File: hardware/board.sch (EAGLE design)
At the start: 79 parts, among them CON1 USB-FPGA1.11, IC1 AD80XX

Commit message: Working on improved board revB Added DC-DC and selection jumper Added some libraries Fixed THS3062 symbol Split up sheets
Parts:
- removed CON_UC: (no value), con-molex:22-23-2061
- added CON2: USB-FPGA-2THT, usb-fpga-2:USB-FPGA-2THT
- added R7: 0R, rcl:R-EU_M0805
- added TP2, TP3, TP_GND2: TPPAD1-13, testpad:TPPAD1-13
- added U$6: IAS0105D09, xppower-IAS01:IAS0105D09
- IC1: value AD80XX -> THS3062; device ad80xx:AD80XX -> ths3062:THS3062
- JP1: device pinhead:PINHD-1X2 -> jumper:JP4Q
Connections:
- removed net N$60: CON1_CDF-FX2.C13~PE3/RXD0OUT, CON_UC-5.S
- removed net N$61: CON1_CDF-FX2.C14~PE2/T2OUT, CON_UC-4.S
- removed net N$62: CON1_CDF-FX2.C15~PE1/T1OUT, CON_UC-3.S
- removed net N$63: CON1_CDF-FX2.C16~PE0/T0OUT, CON_UC-2.S
- new net +9V: JP1.5, U$6.+VOUT
- new net -9V: JP1.7, U$6.-VOUT
- new net N$13: D2.C, JP1.3
- new net N$17: D1.A, JP1.1
- new net N$7: R7.1, U$6.0V
- net +5V: now also U$6.+VIN
- net +5V/3: no longer CON_UC-1.S
- net DAC_OUT_NET: now also TP2.TP; no longer JP1.1
- net GND: now also U$6.-VIN; no longer CON_UC-6.S
- net GND1: now also IC1THS3062OP2.IN+, R7.2, TP3.TP, TP_GND2.TP; no longer IC1AD80XXOP2.IN+, JP1.2
- net N$10: now also IC1THS3062OP1.IN+; no longer IC1AD80XXOP1.IN+
- net N$11: now also IC1THS3062OP1.IN-; no longer IC1AD80XXOP1.IN-
- net N$12: now also IC1THS3062OP1.OUT; no longer IC1AD80XXOP1.OUT
- net N$24: now also IC1THS3062OP2.IN-; no longer IC1AD80XXOP2.IN-
- net N$33: now also IC1THS3062OP2.OUT; no longer IC1AD80XXOP2.OUT
- net V+: no longer OP_VCC.3
- net V-: no longer OP_VCC.1
- net VCC+: now also JP1.4, JP1.6, OP_VCC.3; no longer D2.C
- net VCC-: now also JP1.2, JP1.8, OP_VCC.1; no longer D1.A
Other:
- note added: "Change to v2"
- note added: "Fix library"
- note added: "Gives the unamplified waveform"
- note added: "Power"
- note added: "Select internal/external supply"
- note added: "WARNING: If the FPGA is powered from USB, then the voltage after the reg is usually too low (measured 4.85V) Best is to power FPGA from supply"
- note added: "angled connector? screw connector?"

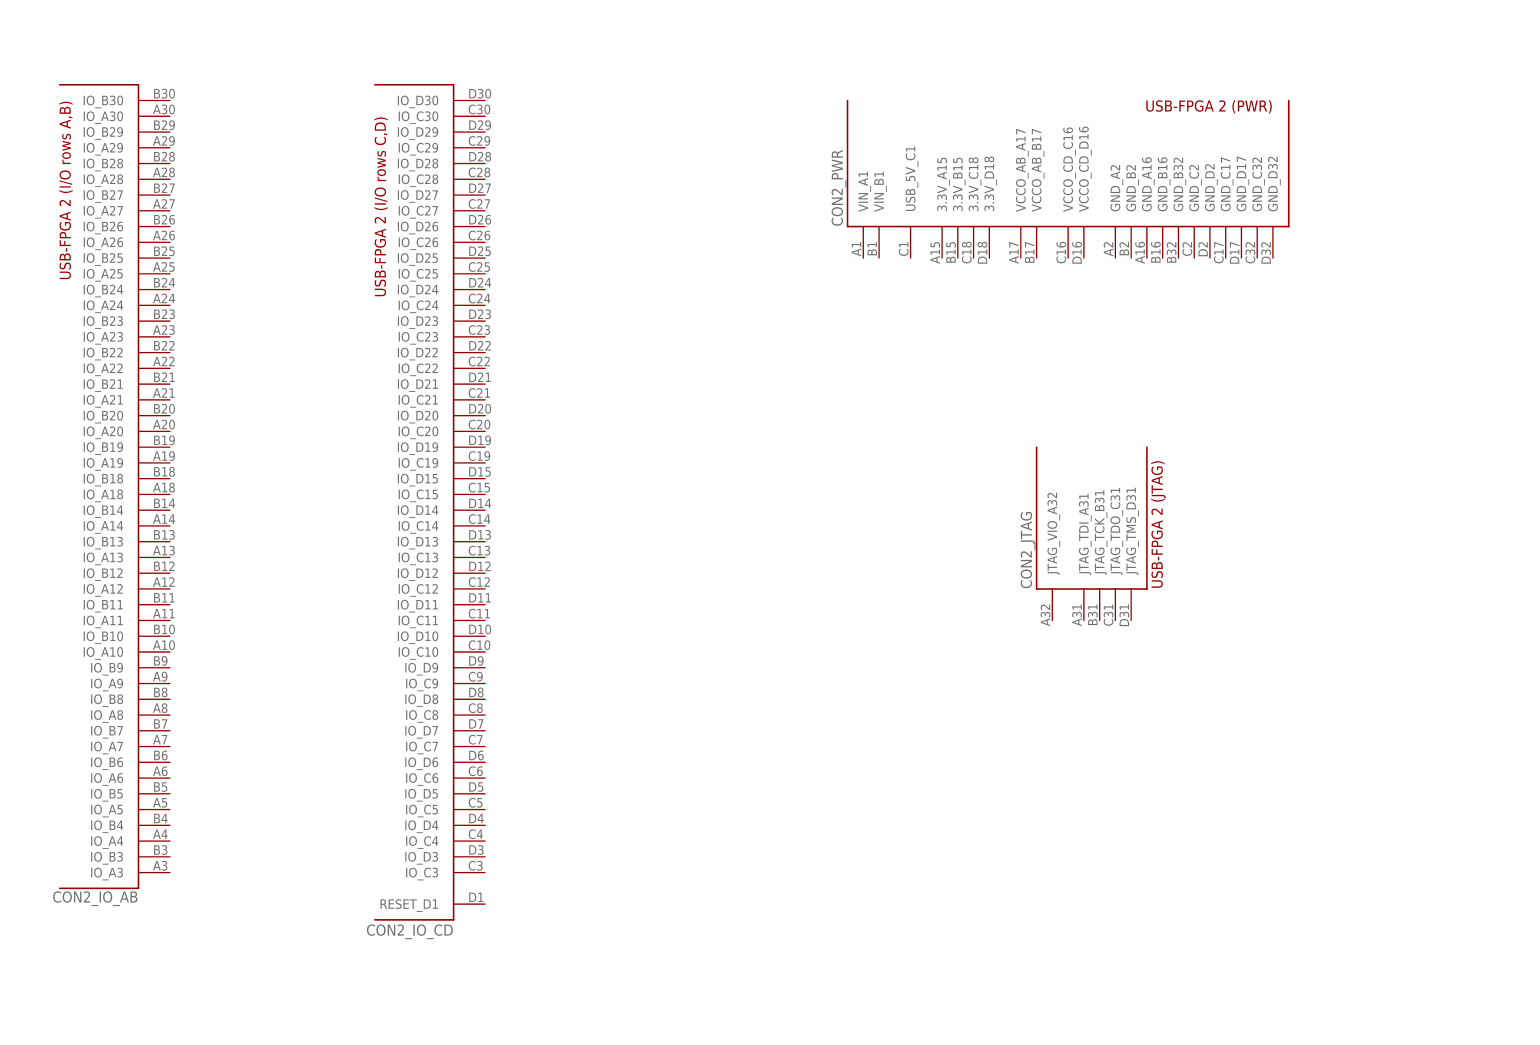
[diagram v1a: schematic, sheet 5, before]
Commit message: Working on change to new v2 pinout
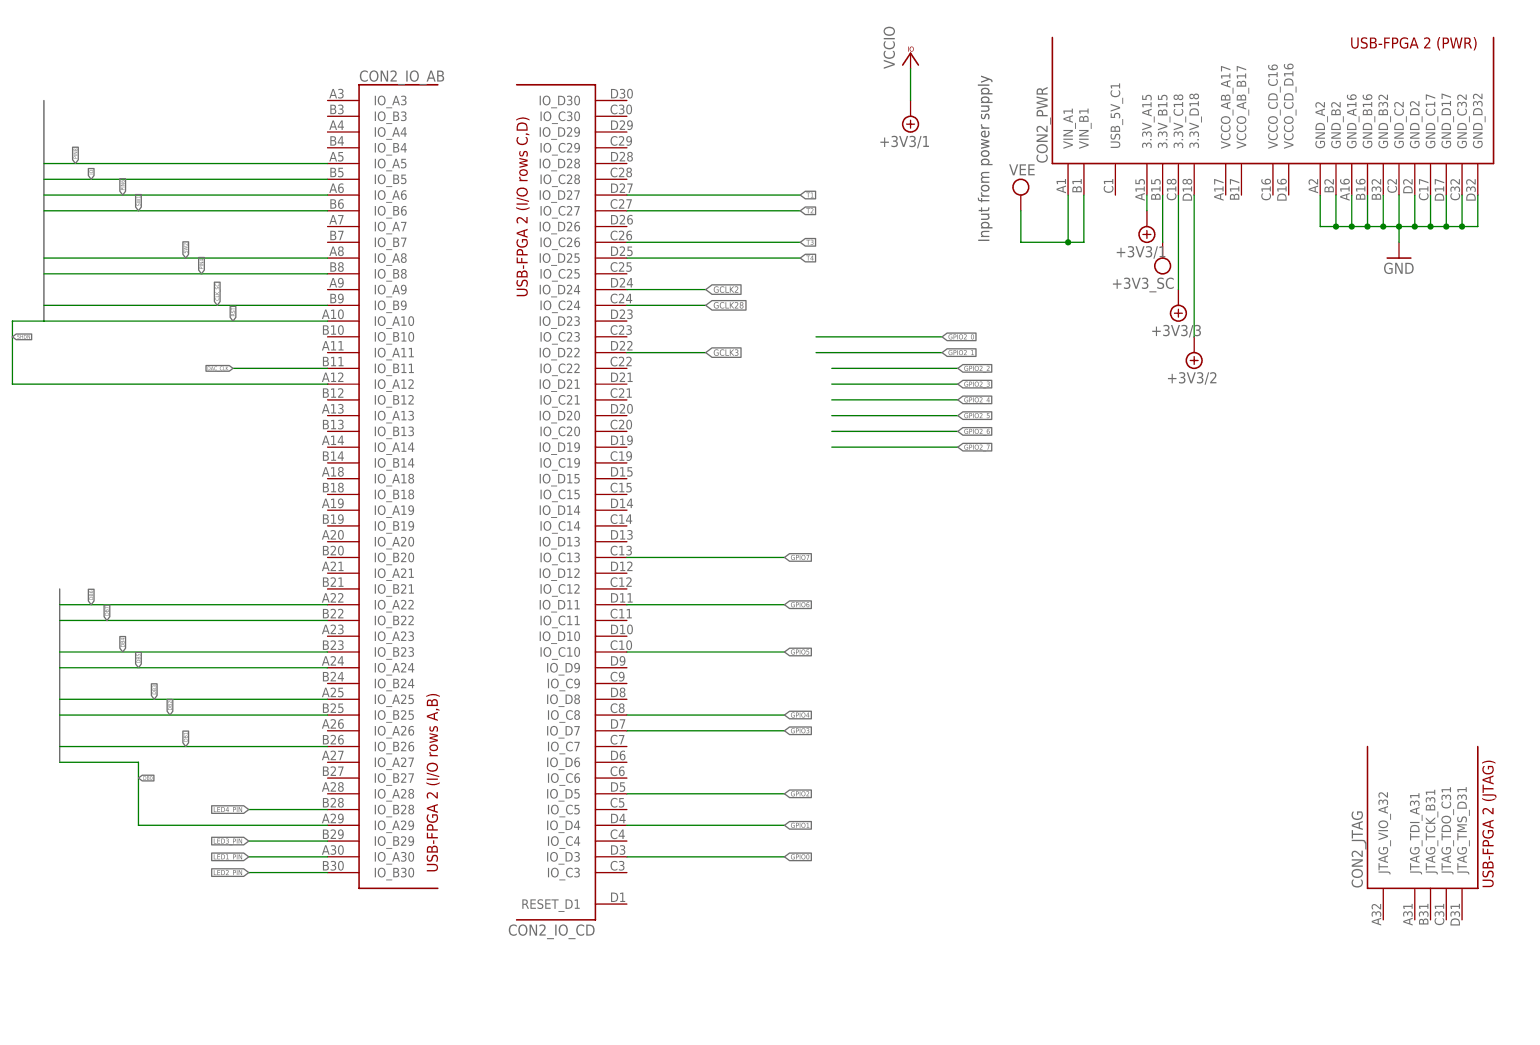
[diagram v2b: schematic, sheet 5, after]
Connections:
- net N$1 renamed GPIO2_0
- net N$2 renamed GPIO2_1
- net N$3 renamed GPIO2_2
- net N$4 renamed GPIO2_3
- net N$5 renamed GPIO2_4
- net N$6 renamed GPIO2_5
- net N$8 renamed GPIO2_6
- net N$9 renamed GPIO2_7
- removed net CLK: AD9708.CLOCK, CON1_ABE-FPGA.A17~C10~IO_L37N_GCLK12_0
- removed net N$25: CON1_CDF-FPGA.D8~K16~IO_L44N_A2_M1DQ7_1, GPIO.3
- removed net N$26: CON1_CDF-FPGA.D9~L16~IO_L47N_LDC_M1DQ1_1, GPIO.4
- removed net N$27: CON1_CDF-FPGA.D10~M16~IO_L46N_FOE_B_M1DQ3_1, GPIO.5
- removed net N$28: CON1_CDF-FPGA.D11~P16~IO_L48N_M1DQ9_1, GPIO.6
- removed net N$29: CON1_CDF-FPGA.D12~P15~IO_L48P_HDC_M1DQ8_1, GPIO.7
- removed net N$30: CON1_CDF-FPGA.D13~T15~IO_L50N_M1UDQSN_1, GPIO.8
- removed net N$31: CON1_CDF-FPGA.D14~K15~IO_L44P_A3_M1DQ6_1, GPIO.9
- removed net N$32: CON1_CDF-FPGA.D15~R14~IO_L50P_M1UDQS_1, GPIO.10
- removed net N$53: CON1_ABE-FPGA.B30~C4~IO_L1P_HSWAPEN_0, R_LED2.2
- removed net N$54: CON1_ABE-FPGA.A30~A4~IO_L1N_VREF_0, R_LED1.2
- removed net N$55: CON1_ABE-FPGA.B29~B5~IO_L2P_0, R_LED3.2
- removed net N$56: CON1_ABE-FPGA.B28~D5~IO_L3P_0, R_LED4.2
- new net DAC_CLK: AD9708.CLOCK, CON1_ABE-FPGA.A17~C10~IO_L37N_GCLK12_0, CON2_IO_AB.IO_B11
- new net GPIO0: CON1_CDF-FPGA.D8~K16~IO_L44N_A2_M1DQ7_1, CON2_IO_CD.IO_D3, GPIO.3
- new net GPIO1: CON1_CDF-FPGA.D9~L16~IO_L47N_LDC_M1DQ1_1, CON2_IO_CD.IO_D4, GPIO.4
- new net GPIO2: CON1_CDF-FPGA.D10~M16~IO_L46N_FOE_B_M1DQ3_1, CON2_IO_CD.IO_D5, GPIO.5
- new net GPIO3: CON1_CDF-FPGA.D11~P16~IO_L48N_M1DQ9_1, CON2_IO_CD.IO_D7, GPIO.6
- new net GPIO4: CON1_CDF-FPGA.D12~P15~IO_L48P_HDC_M1DQ8_1, CON2_IO_CD.IO_C8, GPIO.7
- new net GPIO5: CON1_CDF-FPGA.D13~T15~IO_L50N_M1UDQSN_1, CON2_IO_CD.IO_C10, GPIO.8
- new net GPIO6: CON1_CDF-FPGA.D14~K15~IO_L44P_A3_M1DQ6_1, CON2_IO_CD.IO_D11, GPIO.9
- new net GPIO7: CON1_CDF-FPGA.D15~R14~IO_L50P_M1UDQS_1, CON2_IO_CD.IO_C13, GPIO.10
- new net LED1_PIN: CON1_ABE-FPGA.A30~A4~IO_L1N_VREF_0, CON2_IO_AB.IO_A30, R_LED1.2
- new net LED2_PIN: CON1_ABE-FPGA.B30~C4~IO_L1P_HSWAPEN_0, CON2_IO_AB.IO_B30, R_LED2.2
- new net LED3_PIN: CON1_ABE-FPGA.B29~B5~IO_L2P_0, CON2_IO_AB.IO_B29, R_LED3.2
- new net LED4_PIN: CON1_ABE-FPGA.B28~D5~IO_L3P_0, CON2_IO_AB.IO_B28, R_LED4.2
- net +5V/1: now also CON2_PWR.3.3V_A15
- net +5V/2: now also CON2_PWR.3.3V_D18
- net +5V/3: now also CON2_PWR.3.3V_C18
- net CLK_SC: now also CON2_IO_AB.IO_B9
- net DB0: now also CON2_IO_AB.IO_A29
- net DB1: now also CON2_IO_AB.IO_B26
- net DB2: now also CON2_IO_AB.IO_B25
- net DB3: now also CON2_IO_AB.IO_A25
- net DB4: now also CON2_IO_AB.IO_B23
- net DB5: now also CON2_IO_AB.IO_A24
- net DB6: now also CON2_IO_AB.IO_A22
- net DB7: now also CON2_IO_AB.IO_B22
- net GCLK2: now also CON2_IO_CD.IO_D24
- net GCLK28: now also CON2_IO_CD.IO_C24
- net GCLK3: now also CON2_IO_CD.IO_D22
- net GND: now also CON2_PWR.GND_A16, CON2_PWR.GND_A2, CON2_PWR.GND_B16, CON2_PWR.GND_B2, CON2_PWR.GND_B32, CON2_PWR.GND_C17, CON2_PWR.GND_C2, CON2_PWR.GND_C32, CON2_PWR.GND_D17, CON2_PWR.GND_D2, CON2_PWR.GND_D32
- net IO: now also CON2_IO_AB.IO_B5
- net PIN4: now also CON2_IO_AB.IO_B8
- net PIN6: now also CON2_IO_AB.IO_A6
- net PIN8: now also CON2_IO_AB.IO_A5
- net RST: now also CON2_IO_AB.IO_A10
- net SHDN: now also CON2_IO_AB.IO_A12
- net SW1: now also CON2_IO_AB.IO_B6
- net SW2: now also CON2_IO_AB.IO_A8
- net T1: now also CON2_IO_CD.IO_D27
- net T2: now also CON2_IO_CD.IO_C27
- net T3: now also CON2_IO_CD.IO_C26
- net T4: now also CON2_IO_CD.IO_D25
- net VEE: now also CON2_PWR.VIN_A1, CON2_PWR.VIN_B1
- net VPP: now also CON2_PWR.3.3V_B15
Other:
- note added: "Power / testpads / holes"
- note added: "TODO: * GPIO2 * ADC * check everything * check CLK pins * check GPI0 uC pins Add notes where useful"
- note removed: "Fix library"
- note removed: "Power"
- note removed: "angled connector? screw connector?"
- moved on the sheet: C10, C4, C5, C9, CON2_IO_AB, CON2_IO_CD, CON2_JTAG, CON2_PWR, D1, D2, JP1

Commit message: Added all v2 pins and labels
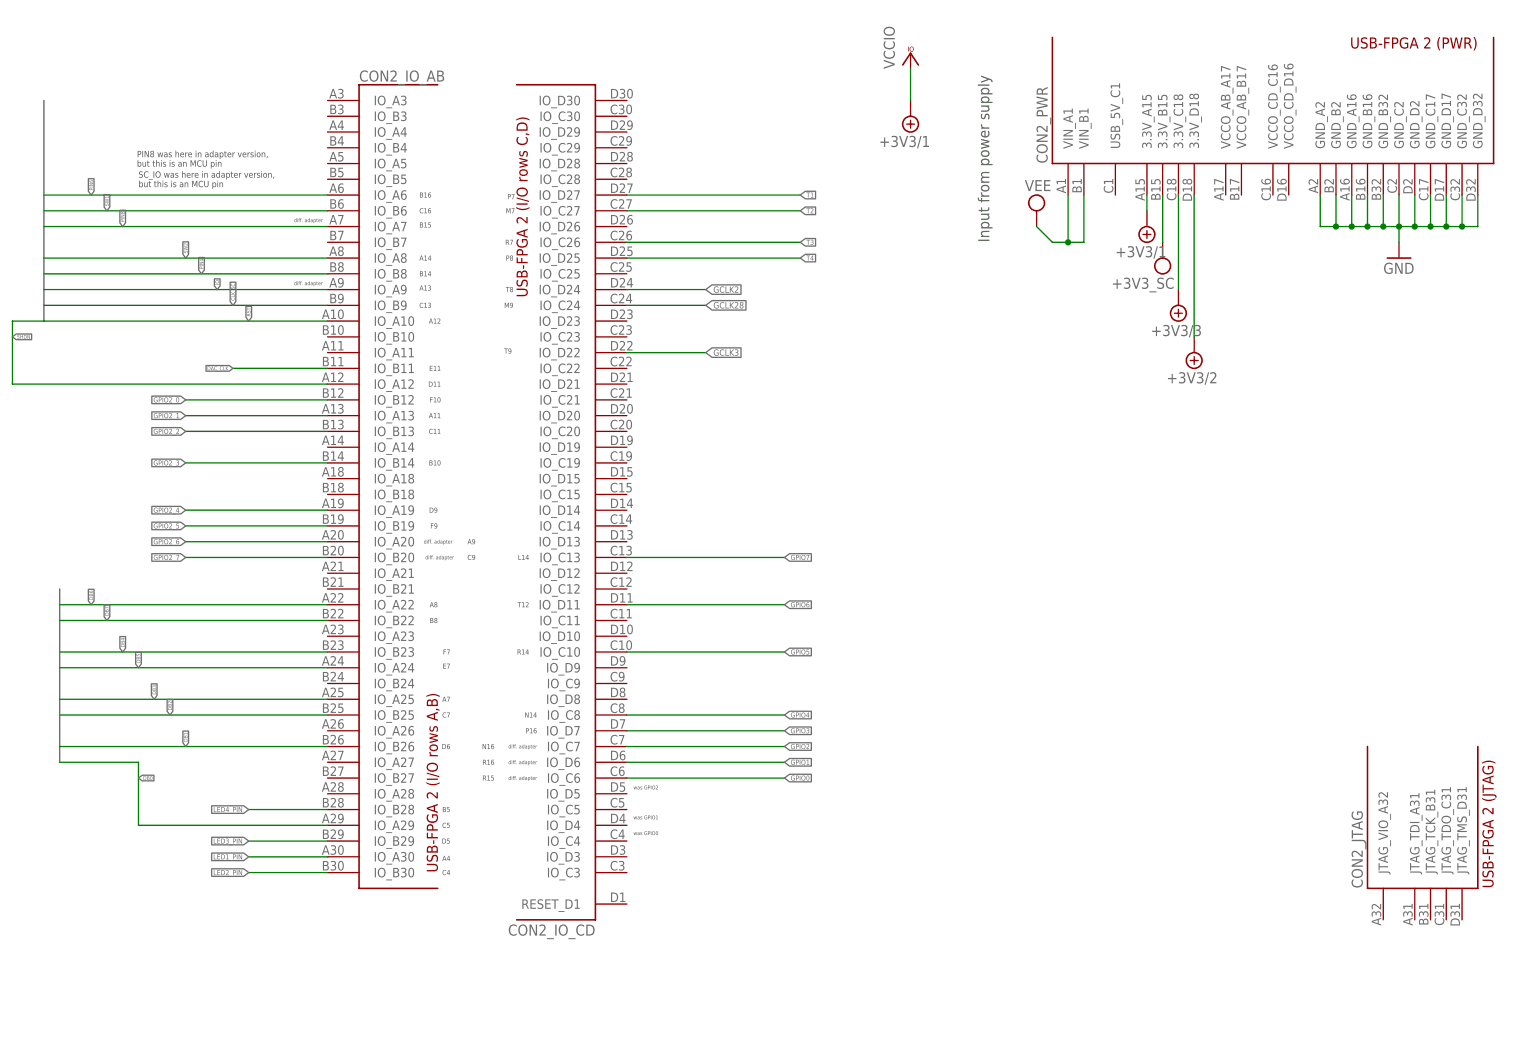
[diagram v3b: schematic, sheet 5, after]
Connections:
- net GPIO0: now also CON2_IO_CD.IO_C6; no longer CON2_IO_CD.IO_D3
- net GPIO1: now also CON2_IO_CD.IO_D6; no longer CON2_IO_CD.IO_D4
- net GPIO2: now also CON2_IO_CD.IO_C7; no longer CON2_IO_CD.IO_D5
- net GPIO2_0: now also CON2_IO_AB.IO_B12
- net GPIO2_1: now also CON2_IO_AB.IO_A13
- net GPIO2_2: now also CON2_IO_AB.IO_B13
- net GPIO2_3: now also CON2_IO_AB.IO_B14
- net GPIO2_4: now also CON2_IO_AB.IO_A19
- net GPIO2_5: now also CON2_IO_AB.IO_B19
- net GPIO2_6: now also CON2_IO_AB.IO_A20
- net GPIO2_7: now also CON2_IO_AB.IO_B20
- net IO: now also CON2_IO_AB.IO_A9; no longer CON2_IO_AB.IO_B5
- net PIN8: now also CON2_IO_AB.IO_A7; no longer CON2_IO_AB.IO_A5
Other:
- note added: "A11"
- note added: "A12"
- note added: "A13"
- note added: "A14"
- note added: "A4"
- note added: "A7"
- note added: "A8"
- note added: "A9"
- note added: "ADC here?"
- note added: "B10"
- note added: "B14"
- note added: "B15"
- note added: "B16"
- note added: "B5"
- note added: "B8"
- note added: "C11"
- note added: "C13"
- note added: "C16"
- note added: "C4"
- note added: "C5"
- note added: "C7"
- note added: "C9"
- note added: "D11"
- note added: "D5"
- note added: "D6"
- note added: "D9"
- note added: "E11"
- note added: "E7"
- note added: "F10"
- note added: "F7"
- note added: "F9"
- note added: "L14"
- note added: "M7"
- note added: "M9"
- note added: "N14"
- note added: "N16"
- note added: "P16"
- note added: "P7"
- note added: "P8"
- note added: "PIN8 was here in adapter version, but this is an MCU pin"
- note added: "R14"
- note added: "R15"
- note added: "R16"
- note added: "R7"
- note added: "SC_IO was here in adapter version, but this is an MCU pin"
- note added: "T12"
- note added: "T8"
- note added: "T9"
- note added: "check, VREF!"
- note added: "diff. adapter"
- note added: "not GCLK"
- note added: "was GPIO0"
- note added: "was GPIO1"
- note added: "was GPIO2"

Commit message: Fully routed (no ADC)
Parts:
- removed CON1: USB-FPGA1.11, usb-fpga-1:USB-FPGA1.11
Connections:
- removed net N$69: CON1_CDF-FPGA.C20~P8~IO_L30P_GCLK1_D13_2
- removed net VCCIO: C19.1, CON1_ABE-PWR.A7~3.3V, GPIO2.1
- net +5V/1: now also C19.1, GPIO2.1; no longer CON1_ABE-PWR.A16~3.3V
- net +5V/2: no longer CON1_CDF-PWR.D6~3.3V
- net +5V/3: no longer CON1_CDF-PWR.C6~3.3V
- net CLK_SC: no longer CON1_ABE-FPGA.A15~E11~IO_L64N_SCP4_0
- net DAC_CLK: no longer CON1_ABE-FPGA.A17~C10~IO_L37N_GCLK12_0
- net DB0: no longer CON1_ABE-FPGA.A29~A5~IO_L2N_0
- net DB1: no longer CON1_ABE-FPGA.A27~A6~IO_L4N_0
- net DB2: no longer CON1_ABE-FPGA.B26~D6~IO_L7P_0
- net DB3: no longer CON1_ABE-FPGA.A26~C6~IO_L7N_0
- net DB4: no longer CON1_ABE-FPGA.A25~E6~IO_L5N_0
- net DB5: no longer CON1_ABE-FPGA.B25~F7~IO_L5P_0
- net DB6: no longer CON1_ABE-FPGA.A24~A7~IO_L6N_0
- net DB7: no longer CON1_ABE-FPGA.B24~C7~IO_L6P_0
- net GCLK2: no longer CON1_CDF-FPGA.D22~N8~IO_L29N_GCLK2_2
- net GCLK28: no longer CON1_CDF-FPGA.C22~T7~IO_L32N_GCLK28_2
- net GCLK3: no longer CON1_CDF-FPGA.C21~M9~IO_L29P_GCLK3_2
- net GND: no longer CON1_ABE-PWR.A21~GND, CON1_ABE-PWR.A2~GND, CON1_ABE-PWR.A32~GND, CON1_ABE-PWR.B13~GND, CON1_ABE-PWR.B21~GND, CON1_ABE-PWR.B2~GND, CON1_ABE-PWR.B32~GND, CON1_ABE-PWR.B5~GND, CON1_CDF-PWR.C17~GND, CON1_CDF-PWR.C26~GND, CON1_CDF-PWR.C32~GND, CON1_CDF-PWR.C4~GND, CON1_CDF-PWR.C8~GND, CON1_CDF-PWR.D26~GND, CON1_CDF-PWR.D4~GND
- net GPIO0: no longer CON1_CDF-FPGA.D8~K16~IO_L44N_A2_M1DQ7_1
- net GPIO1: no longer CON1_CDF-FPGA.D9~L16~IO_L47N_LDC_M1DQ1_1
- net GPIO2: no longer CON1_CDF-FPGA.D10~M16~IO_L46N_FOE_B_M1DQ3_1
- net GPIO2_0: no longer CON1_ABE-FPGA.A13~C13~IO_L63P_SCP7_0
- net GPIO2_1: no longer CON1_ABE-FPGA.A18~B12~IO_L62P_0
- net GPIO2_2: no longer CON1_ABE-FPGA.B18~A12~IO_L62N_VREF_0
- net GPIO2_3: no longer CON1_ABE-FPGA.A19~A9~IO_L34N_GCLK18_0
- net GPIO2_4: no longer CON1_ABE-FPGA.A20~C8~IO_L38N_VREF_0
- net GPIO2_5: no longer CON1_ABE-FPGA.B20~D8~IO_L38P_0
- net GPIO2_6: no longer CON1_ABE-FPGA.B27~B6~IO_L4P_0
- net GPIO2_7: no longer CON1_ABE-FPGA.A28~C5~IO_L3N_0
- net GPIO3: no longer CON1_CDF-FPGA.D11~P16~IO_L48N_M1DQ9_1
- net GPIO4: no longer CON1_CDF-FPGA.D12~P15~IO_L48P_HDC_M1DQ8_1
- net GPIO5: no longer CON1_CDF-FPGA.D13~T15~IO_L50N_M1UDQSN_1
- net GPIO6: no longer CON1_CDF-FPGA.D14~K15~IO_L44P_A3_M1DQ6_1
- net GPIO7: no longer CON1_CDF-FPGA.D15~R14~IO_L50P_M1UDQS_1
- net IO: no longer CON1_ABE-FPGA.B9~B16~IO_L29N_A22_M1A14_1
- net LED1_PIN: no longer CON1_ABE-FPGA.A30~A4~IO_L1N_VREF_0
- net LED2_PIN: no longer CON1_ABE-FPGA.B30~C4~IO_L1P_HSWAPEN_0
- net LED3_PIN: no longer CON1_ABE-FPGA.B29~B5~IO_L2P_0
- net LED4_PIN: no longer CON1_ABE-FPGA.B28~D5~IO_L3P_0
- net PIN4: no longer CON1_ABE-FPGA.B14~D11~IO_L66P_SCP1_0
- net PIN6: no longer CON1_ABE-FPGA.A12~A14~IO_L65N_SCP2_0
- net PIN8: no longer CON1_ABE-FPGA.A9~B15~IO_L29P_A23_M1A13_1
- net RST: no longer CON1_ABE-FPGA.B15~F10~IO_L64P_SCP5_0
- net SHDN: no longer CON1_ABE-FPGA.B17~E10~IO_L37P_GCLK13_0
- net SW1: no longer CON1_ABE-FPGA.B12~B14~IO_L65P_SCP3_0
- net SW2: no longer CON1_ABE-FPGA.A14~D12~IO_L66N_SCP0_0
- net T1: no longer CON1_CDF-FPGA.D24~P6~IO_L47P_2
- net T2: no longer CON1_CDF-FPGA.C24~N6~IO_L64N_D9_2
- net T3: no longer CON1_CDF-FPGA.D23~P7~IO_L31P_GCLK31_D14_2
- net T4: no longer CON1_CDF-FPGA.C23~M7~IO_L31N_GCLK30_D15_2
- net VEE: no longer CON1_ABE-PWR.A1~4..35V, CON1_ABE-PWR.B1~4..35V
- net VPP: no longer CON1_ABE-PWR.B16~3.3V
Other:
- note added: "Connect so that FPGA has to start DAC?"
- note added: "DAC"
- note removed: "Analog mux useful if we only have 3.3 / 5 / GND (no ext supply)"
- note removed: "Change to v2"
- note removed: "DAC, LEDs, GPIO"
- note removed: "Power & JTAG & Misc"
- note removed: "TODO: Clock glitching output and/or maybe analog mux?"
